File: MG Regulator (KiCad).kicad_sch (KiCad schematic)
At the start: 20 parts, among them J1 10K thermistor connector, Q1 AM2336N-CT, Q2 AM2336N-CT, T1 B+, T2 +, T3 -, T4 F, U1 AP7370-50FDC, U2 ACS723LLCTR-10AU-T

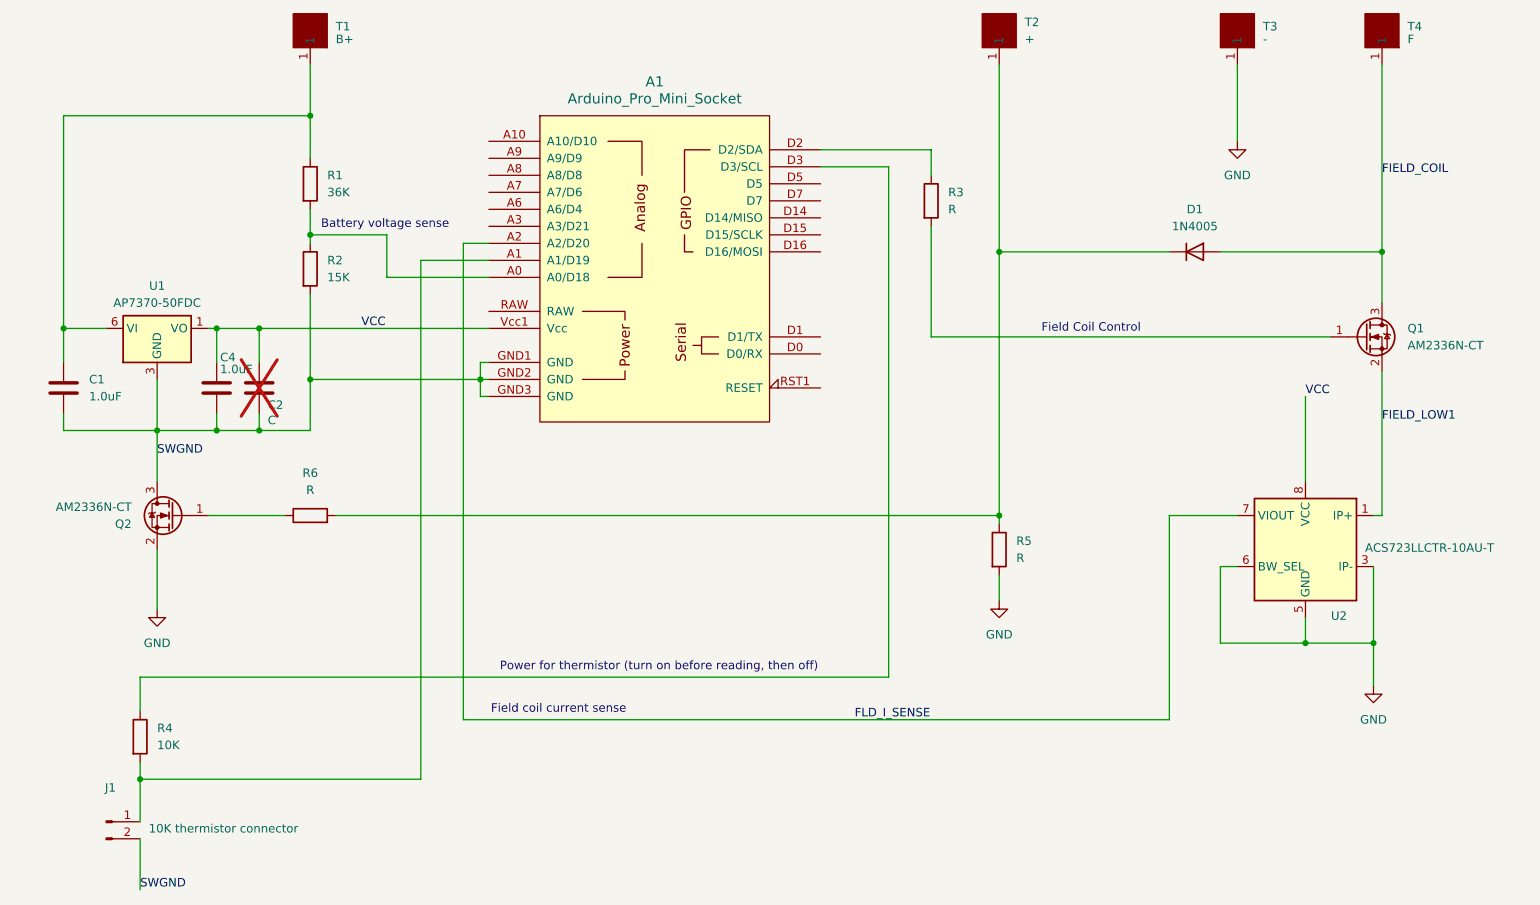
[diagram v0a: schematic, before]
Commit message: Modified to be able to control the ignition led and enable arduino power from the ignition switch.
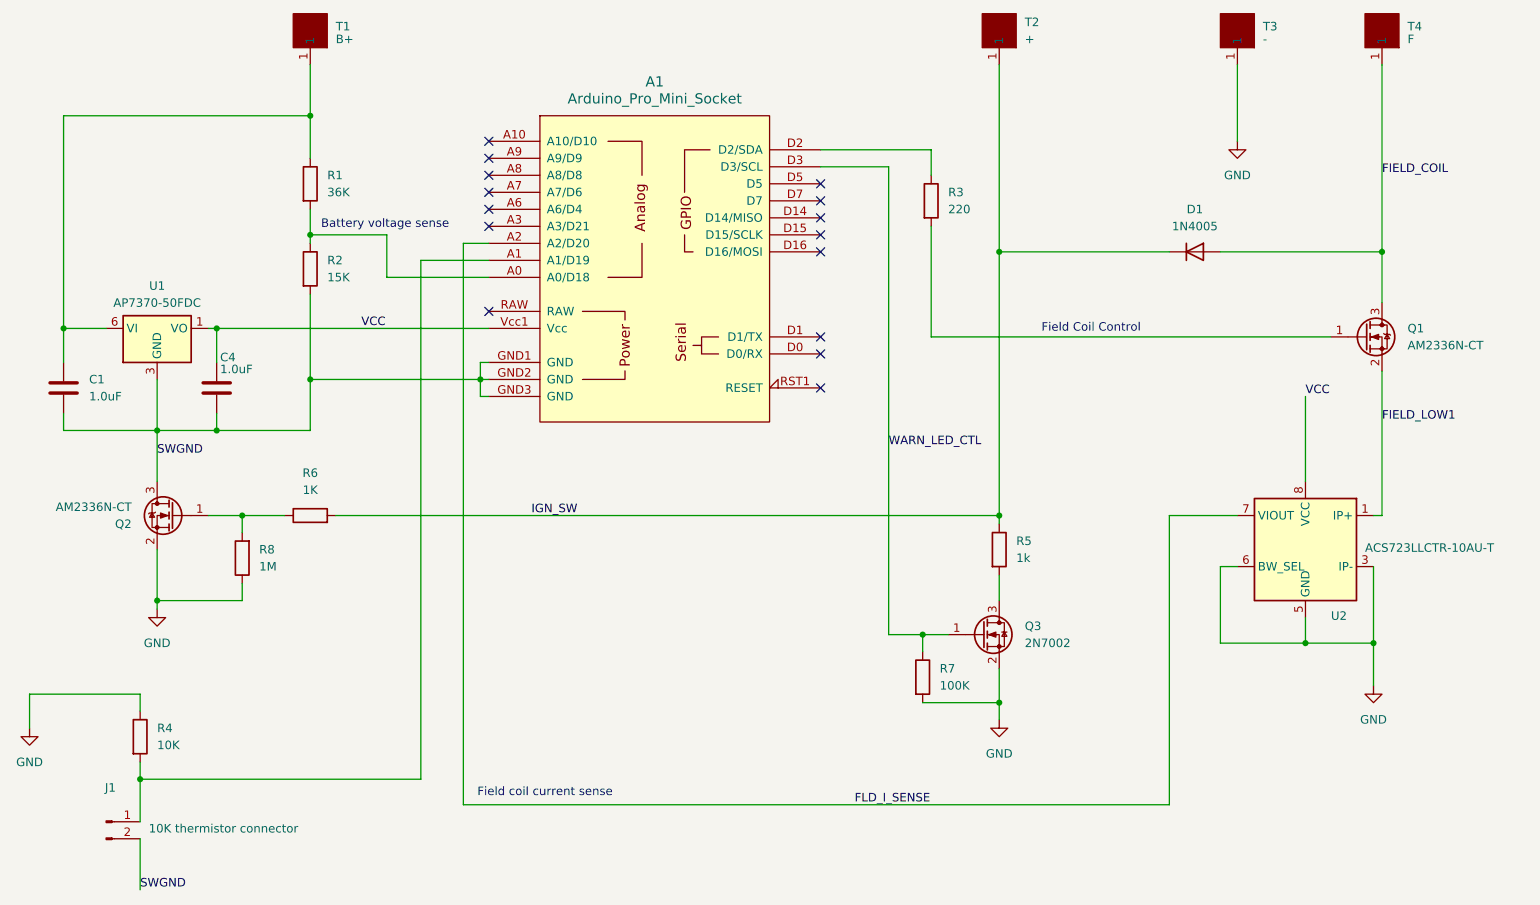
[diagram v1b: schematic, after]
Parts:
- removed C2: C, Capacitor_SMD:C_0805_2012Metric_Pad1.18x1.45mm_HandSolder, symbol Device:C
- added Q3: 2N7002, Package_TO_SOT_SMD:SOT-23, symbol Transistor_FET:2N7002
- added R7: 100K, Resistor_SMD:R_0805_2012Metric, symbol Device:R
- added R8: 1M, Resistor_SMD:R_0805_2012Metric, symbol Device:R
- R3: value R -> 220
- R5: value R -> 1k
- R6: value R -> 1K
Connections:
- net GND: now also R4.1, Q3.2 (S), R7.2, R8.1; no longer R5.2
- net IGN_SW: now reaches D1.1 (K), R5.1, R6.2, T2.1
- net WARN_LED_CTL: now reaches A1.D3 (D3/SCL)
- net WARN_LED_CTL: now also Q3.1 (G), R7.1; no longer R4.1
- net at Q2.1 (G), R6.1: now also R8.2
- new net: Q3.3 (D), R5.2
- no-connect marks 0 -> 15
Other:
- note removed: "Power for thermistor (turn on before reading, then off)"

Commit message: Changed the fets to be the same.  Fixed the problem with the thermistor not being powered.  (this fix isn't on the boards ordered)
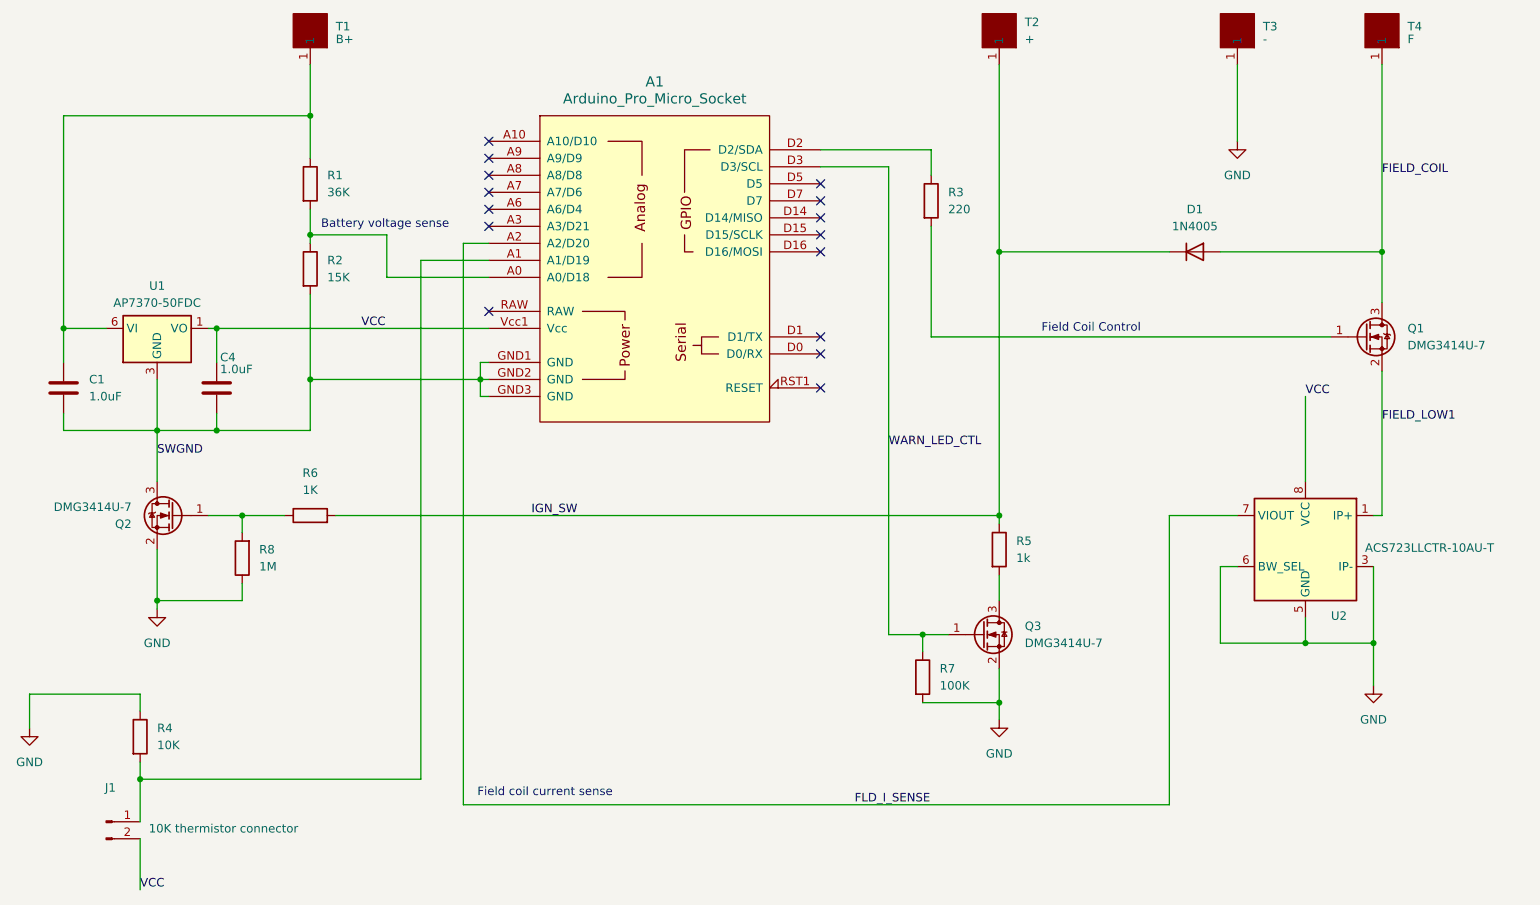
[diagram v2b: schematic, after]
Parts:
- A1: value Arduino_Pro_Mini_Socket -> Arduino_Pro_Micro_Socket
- Q1, Q2: value AM2336N-CT -> DMG3414U-7
- Q3: value 2N7002 -> DMG3414U-7
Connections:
- net SWGND: no longer J1.2 (Pin_2)
- net VCC: now also J1.2 (Pin_2)
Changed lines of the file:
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@@
 		)
 	)
-	(label "SWGND"
+	(label "VCC"
 		(at 63.5 173.99 0)
 		(effects
@@
 			)
 		)
-		(property "Value" "Arduino_Pro_Mini_Socket"
+		(property "Value" "Arduino_Pro_Micro_Socket"
 			(at 140.335 55.88 0)
 			(show_name no)
@@
 			)
 		)
-		(property "Value" "2N7002"
+		(property "Value" "DMG3414U-7"
 			(at 195.58 137.1599 0)
 			(show_name no)
@@
 			)
 		)
-		(property "Value" "AM2336N-CT"
+		(property "Value" "DMG3414U-7"
 			(at 62.23 116.8401 0)
 			(show_name no)
@@
 			)
 		)
-		(property "Value" "AM2336N-CT"
+		(property "Value" "DMG3414U-7"
 			(at 252.73 92.7099 0)
 			(show_name no)
